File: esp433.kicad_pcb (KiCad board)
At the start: 2 copper layers, 47.1 x 72.6 mm, 50 parts, among them J1 USB_OTG, J2 CONN_01X03, Q1 MBT2222ADW1T1, SW1 SW_Push, U1 IRM-02-5, U2 AP2127K-3.3, U3 MAX7044, U4 ESP-12E, U5 FT231XS, Y1 Crystal

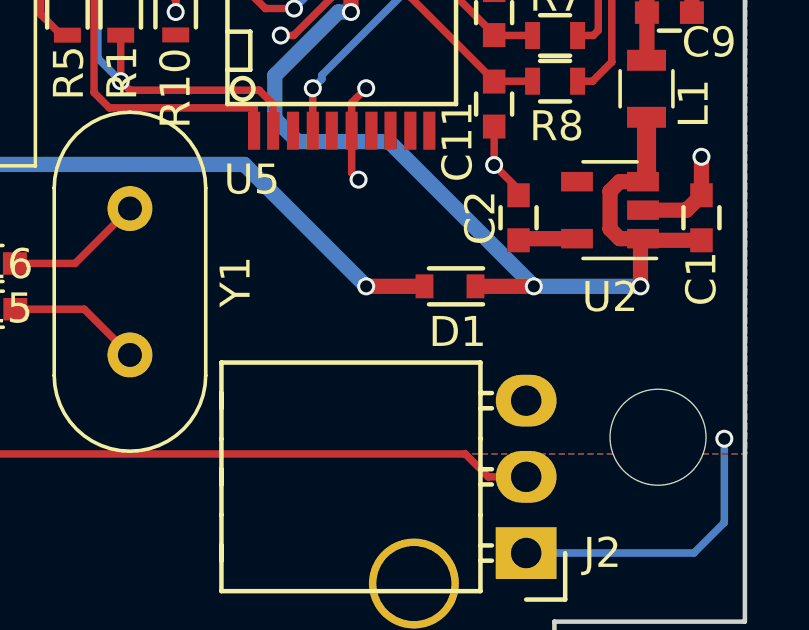
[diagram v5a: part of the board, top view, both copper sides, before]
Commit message: Fix footprint for D1
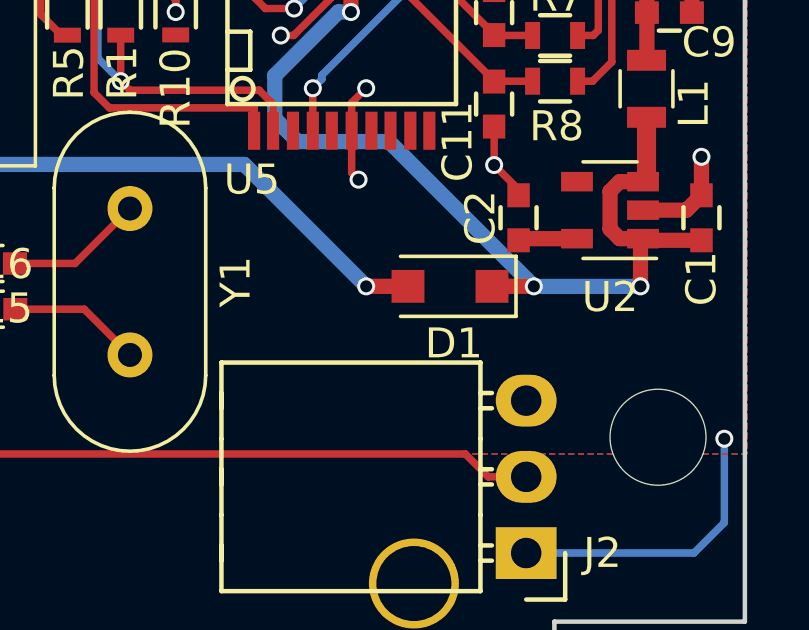
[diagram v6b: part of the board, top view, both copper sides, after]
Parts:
- D1: footprint Diodes_SMD:D_0603 -> Diodes_SMD:D_SOD-123F
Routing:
- net Net-(D1-Pad2): track 27.6 -> 27.1 mm
- net +5V: track 39.9 -> 39.3 mm
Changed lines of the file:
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@@
   (general
     (links 93)
-    (no_connects 6)
+    (no_connects 0)
     (area 90.679199 65.202999 137.920801 137.997001)
     (thickness 1.6)
@@
     )
   )
-  (module Diodes_SMD:D_0603 (layer F.Cu)
-    (at 128.016 120.396 180)
-    (descr "Diode SMD in 0603 package")
-    (tags "smd diode")
-    (attr smd)
-    (fp_text reference D1 (at -0.254 -1.524 180) (layer F.SilkS)
-      (effects (font (size 1 1) (thickness 0.15)))
-    )
-    (fp_text value D (at -2.032 0 180) (layer F.Fab)
-      (effects (font (size 1 1) (thickness 0.15)))
-    )
-    (fp_line (start 1.5 0.8) (end 1.5 -0.8) (layer F.CrtYd) (width 0.05))
-    (fp_line (start -1.5 0.8) (end 1.5 0.8) (layer F.CrtYd) (width 0.05))
-    (fp_line (start -1.5 -0.8) (end -1.5 0.8) (layer F.CrtYd) (width 0.05))
-    (fp_line (start 1.5 -0.8) (end -1.5 -0.8) (layer F.CrtYd) (width 0.05))
-    (fp_line (start 0.2 0) (end 0.4 0) (layer F.Fab) (width 0.15))
-    (fp_line (start -0.1 0) (end -0.3 0) (layer F.Fab) (width 0.15))
-    (fp_line (start -0.1 -0.2) (end -0.1 0.2) (layer F.Fab) (width 0.15))
-    (fp_line (start 0.2 0.2) (end 0.2 -0.2) (layer F.Fab) (width 0.15))
-    (fp_line (start -0.1 0) (end 0.2 0.2) (layer F.Fab) (width 0.15))
-    (fp_line (start 0.2 -0.2) (end -0.1 0) (layer F.Fab) (width 0.15))
-    (fp_line (start -0.8 0.5) (end -0.8 -0.5) (layer F.Fab) (width 0.15))
-    (fp_line (start 0.8 0.5) (end -0.8 0.5) (layer F.Fab) (width 0.15))
-    (fp_line (start 0.8 -0.5) (end 0.8 0.5) (layer F.Fab) (width 0.15))
-    (fp_line (start -0.8 -0.5) (end 0.8 -0.5) (layer F.Fab) (width 0.15))
-    (fp_line (start -1.1 0.6) (end 0.7 0.6) (layer F.SilkS) (width 0.15))
-    (fp_line (start -1.1 -0.6) (end 0.7 -0.6) (layer F.SilkS) (width 0.15))
-    (pad 1 smd rect (at -0.85 0 180) (size 0.6 0.8) (layers F.Cu F.Paste F.Mask)
-      (net 4 +5V))
-    (pad 2 smd rect (at 0.85 0 180) (size 0.6 0.8) (layers F.Cu F.Paste F.Mask)
-      (net 5 "Net-(D1-Pad2)"))
-  )
   (module LEDs:LED_0603 (layer F.Cu)
     (at 135.382 93.218 90)
@@
       (net 35 "Net-(C17-Pad1)"))
     (model Capacitors_SMD.3dshapes/C_0603.wrl
+      (at (xyz 0 0 0))
+      (scale (xyz 1 1 1))
+      (rotate (xyz 0 0 0))
+    )
+  )
+  (module Diodes_SMD:D_SOD-123F (layer F.Cu)
+    (at 128.016 120.396 180)
+    (descr D_SOD-123F)
+    (tags D_SOD-123F)
+    (attr smd)
+    (fp_text reference D1 (at -0.127 -1.905 180) (layer F.SilkS)
+      (effects (font (size 1 1) (thickness 0.15)))
+    )
+    (fp_text value D (at 0 2.1 180) (layer F.Fab)
+      (effects (font (size 1 1) (thickness 0.15)))
+    )
+    (fp_text user %R (at -0.127 -1.905 180) (layer F.Fab)
+      (effects (font (size 1 1) (thickness 0.15)))
+    )
+    (fp_line (start -2.2 -1) (end -2.2 1) (layer F.SilkS) (width 0.12))
+    (fp_line (start 0.25 0) (end 0.75 0) (layer F.Fab) (width 0.1))
+    (fp_line (start 0.25 0.4) (end -0.35 0) (layer F.Fab) (width 0.1))
+    (fp_line (start 0.25 -0.4) (end 0.25 0.4) (layer F.Fab) (width 0.1))
+    (fp_line (start -0.35 0) (end 0.25 -0.4) (layer F.Fab) (width 0.1))
+    (fp_line (start -0.35 0) (end -0.35 0.55) (layer F.Fab) (width 0.1))
+    (fp_line (start -0.35 0) (end -0.35 -0.55) (layer F.Fab) (width 0.1))
+    (fp_line (start -0.75 0) (end -0.35 0) (layer F.Fab) (width 0.1))
+    (fp_line (start -1.4 0.9) (end -1.4 -0.9) (layer F.Fab) (width 0.1))
+    (fp_line (start 1.4 0.9) (end -1.4 0.9) (layer F.Fab) (width 0.1))
+    (fp_line (start 1.4 -0.9) (end 1.4 0.9) (layer F.Fab) (width 0.1))
+    (fp_line (start -1.4 -0.9) (end 1.4 -0.9) (layer F.Fab) (width 0.1))
+    (fp_line (start -2.2 -1.15) (end 2.2 -1.15) (layer F.CrtYd) (width 0.05))
+    (fp_line (start 2.2 -1.15) (end 2.2 1.15) (layer F.CrtYd) (width 0.05))
+    (fp_line (start 2.2 1.15) (end -2.2 1.15) (layer F.CrtYd) (width 0.05))
+    (fp_line (start -2.2 -1.15) (end -2.2 1.15) (layer F.CrtYd) (width 0.05))
+    (fp_line (start -2.2 1) (end 1.65 1) (layer F.SilkS) (width 0.12))
+    (fp_line (start -2.2 -1) (end 1.65 -1) (layer F.SilkS) (width 0.12))
+    (pad 1 smd rect (at -1.4 0 180) (size 1.1 1.1) (layers F.Cu F.Paste F.Mask)
+      (net 4 +5V))
+    (pad 2 smd rect (at 1.4 0 180) (size 1.1 1.1) (layers F.Cu F.Paste F.Mask)
+      (net 5 "Net-(D1-Pad2)"))
+    (model ${KISYS3DMOD}/Diodes_SMD.3dshapes/D_SOD-123F.wrl
       (at (xyz 0 0 0))
       (scale (xyz 1 1 1))
@@
   (segment (start 130.769145 113.557891) (end 129.499145 113.557891) (width 0.25) (layer F.Cu) (net 3))
   (segment (start 129.499145 113.557891) (end 129.487145 113.569891) (width 0.25) (layer F.Cu) (net 3))
-  (segment (start 128.866 120.396) (end 130.81 120.396) (width 0.508) (layer F.Cu) (net 4))
+  (segment (start 130.81 120.396) (end 129.416 120.396) (width 0.508) (layer F.Cu) (net 4))
   (via (at 130.81 120.396) (size 0.6) (drill 0.4) (layers F.Cu B.Cu) (net 4))
   (segment (start 122.174 114.808) (end 122.936 115.57) (width 0.508) (layer B.Cu) (net 4))
@@
   (segment (start 124.525344 108.77789) (end 124.737345 108.989891) (width 0.381) (layer F.Cu) (net 4))
   (segment (start 123.945144 108.77789) (end 124.525344 108.77789) (width 0.381) (layer F.Cu) (net 4))
+  (segment (start 125.222 120.396) (end 126.616 120.396) (width 0.508) (layer F.Cu) (net 5))
   (segment (start 114.554 116.332) (end 121.158 116.332) (width 0.508) (layer B.Cu) (net 5))
   (via (at 125.222 120.396) (size 0.6) (drill 0.4) (layers F.Cu B.Cu) (net 5))
   (segment (start 114.554 116.332) (end 105.898 116.332) (width 0.508) (layer B.Cu) (net 5))
   (segment (start 105.898 116.332) (end 102.596 113.03) (width 0.508) (layer B.Cu) (net 5))
-  (segment (start 125.222 120.396) (end 127.166 120.396) (width 0.508) (layer F.Cu) (net 5))
   (segment (start 121.158 116.332) (end 125.222 120.396) (width 0.508) (layer B.Cu) (net 5))
   (segment (start 102.907 124.46) (end 104.431 122.936) (width 0.25) (layer F.Cu) (net 6))

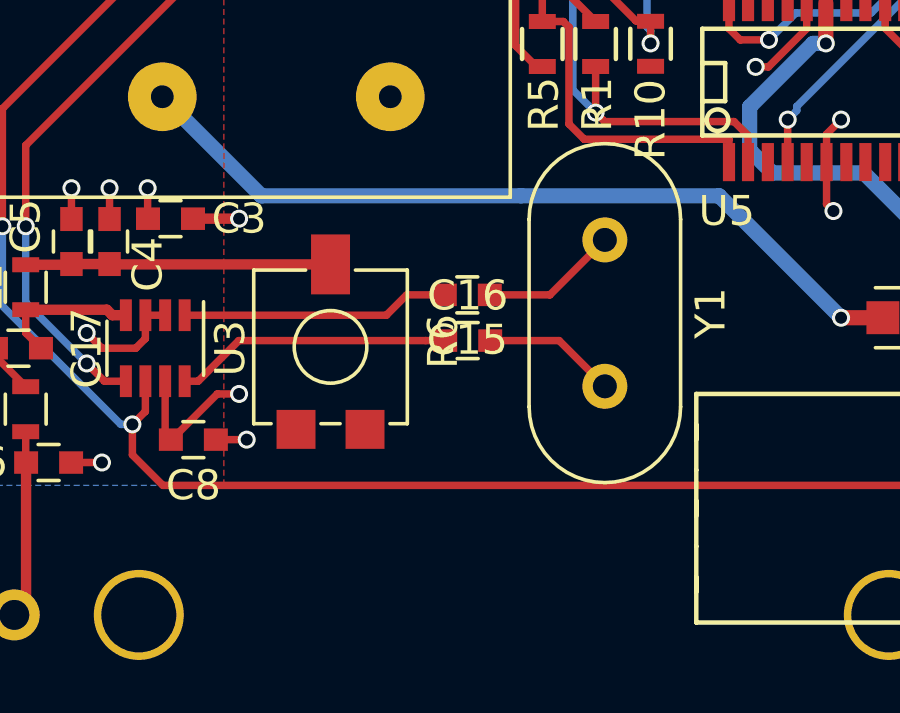
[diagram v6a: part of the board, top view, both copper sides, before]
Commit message: Add some dnp footprints for additional oscillator parallel capacitance
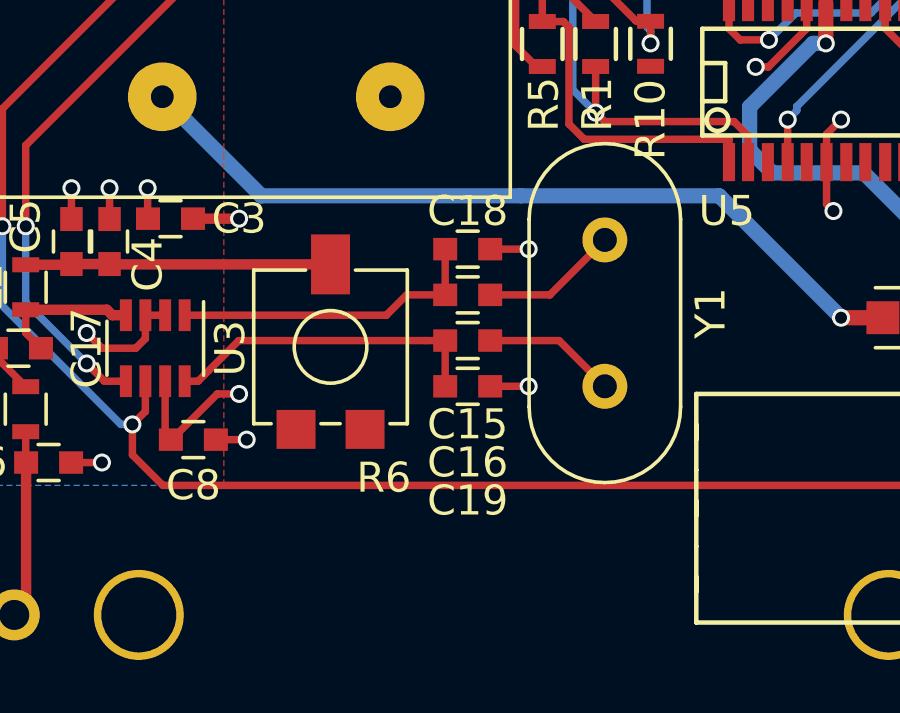
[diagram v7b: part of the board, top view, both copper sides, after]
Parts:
- added C18: DNP, Capacitors_SMD:C_0603, F.Cu at (112.8, 118.1)
- added C19: DNP, Capacitors_SMD:C_0603, F.Cu at (112.8, 122.7)
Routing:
- net GND: track 46.1 -> 48.7 mm, vias 21 -> 23
- net Net-(C15-Pad2): track 8.95 -> 10.5 mm
- net Net-(C16-Pad1): track 9.57 -> 11.1 mm
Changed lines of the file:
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@@
 (kicad_pcb (version 4) (host pcbnew 4.0.7)
   (general
-    (links 93)
-    (no_connects 0)
+    (links 97)
+    (no_connects 3)
     (area 90.679199 65.202999 137.920801 137.997001)
     (thickness 1.6)
-    (drawings 20)
-    (tracks 325)
+    (drawings 22)
+    (tracks 331)
     (zones 0)
-    (modules 50)
+    (modules 52)
     (nets 36)
   )
@@
     (tags "Spindle Trimmer Potentiometer   Vishay TS53YL")
     (attr smd)
-    (fp_text reference R6 (at -0.18 -3.75 270) (layer F.SilkS)
+    (fp_text reference R6 (at 4.362 -1.778 540) (layer F.SilkS)
       (effects (font (size 1 1) (thickness 0.15)))
     )
@@
   )
   (module Capacitors_SMD:C_0603 (layer F.Cu)
-    (at 112.764 119.634 180)
+    (at 112.776 119.634 180)
     (descr "Capacitor SMD 0603, reflow soldering, AVX (see smccp.pdf)")
     (tags "capacitor 0603")
     (attr smd)
-    (fp_text reference C15 (at 0 -1.5 180) (layer F.SilkS)
+    (fp_text reference C15 (at 0 -4.318 180) (layer F.SilkS)
       (effects (font (size 1 1) (thickness 0.15)))
     )
@@
     (tags "capacitor 0603")
     (attr smd)
-    (fp_text reference C16 (at 0 -1.5) (layer F.SilkS)
+    (fp_text reference C16 (at 0 4.064) (layer F.SilkS)
       (effects (font (size 1 1) (thickness 0.15)))
     )
@@
     )
   )
+  (module Capacitors_SMD:C_0603 (layer F.Cu)
+    (at 112.776 118.11 180)
+    (descr "Capacitor SMD 0603, reflow soldering, AVX (see smccp.pdf)")
+    (tags "capacitor 0603")
+    (attr smd)
+    (fp_text reference C18 (at 0 1.27 180) (layer F.SilkS)
+      (effects (font (size 1 1) (thickness 0.15)))
+    )
+    (fp_text value DNP (at 0 1.5 180) (layer F.Fab)
+      (effects (font (size 1 1) (thickness 0.15)))
+    )
+    (fp_line (start 1.4 0.65) (end -1.4 0.65) (layer F.CrtYd) (width 0.05))
+    (fp_line (start 1.4 0.65) (end 1.4 -0.65) (layer F.CrtYd) (width 0.05))
+    (fp_line (start -1.4 -0.65) (end -1.4 0.65) (layer F.CrtYd) (width 0.05))
+    (fp_line (start -1.4 -0.65) (end 1.4 -0.65) (layer F.CrtYd) (width 0.05))
+    (fp_line (start 0.35 0.6) (end -0.35 0.6) (layer F.SilkS) (width 0.12))
+    (fp_line (start -0.35 -0.6) (end 0.35 -0.6) (layer F.SilkS) (width 0.12))
+    (fp_line (start -0.8 -0.4) (end 0.8 -0.4) (layer F.Fab) (width 0.1))
+    (fp_line (start 0.8 -0.4) (end 0.8 0.4) (layer F.Fab) (width 0.1))
+    (fp_line (start 0.8 0.4) (end -0.8 0.4) (layer F.Fab) (width 0.1))
+    (fp_line (start -0.8 0.4) (end -0.8 -0.4) (layer F.Fab) (width 0.1))
+    (fp_text user %R (at 0 0 180) (layer F.Fab)
+      (effects (font (size 0.3 0.3) (thickness 0.075)))
+    )
+    (pad 2 smd rect (at 0.75 0 180) (size 0.8 0.75) (layers F.Cu F.Paste F.Mask)
+      (net 31 "Net-(C15-Pad2)"))
+    (pad 1 smd rect (at -0.75 0 180) (size 0.8 0.75) (layers F.Cu F.Paste F.Mask)
+      (net 1 GND))
+    (model Capacitors_SMD.3dshapes/C_0603.wrl
+      (at (xyz 0 0 0))
+      (scale (xyz 1 1 1))
+      (rotate (xyz 0 0 0))
+    )
+  )
+  (module Capacitors_SMD:C_0603 (layer F.Cu)
+    (at 112.776 122.682 180)
+    (descr "Capacitor SMD 0603, reflow soldering, AVX (see smccp.pdf)")
+    (tags "capacitor 0603")
+    (attr smd)
+    (fp_text reference C19 (at 0 -3.81 180) (layer F.SilkS)
+      (effects (font (size 1 1) (thickness 0.15)))
+    )
+    (fp_text value DNP (at 0 1.5 180) (layer F.Fab)
+      (effects (font (size 1 1) (thickness 0.15)))
+    )
+    (fp_line (start 1.4 0.65) (end -1.4 0.65) (layer F.CrtYd) (width 0.05))
+    (fp_line (start 1.4 0.65) (end 1.4 -0.65) (layer F.CrtYd) (width 0.05))
+    (fp_line (start -1.4 -0.65) (end -1.4 0.65) (layer F.CrtYd) (width 0.05))
+    (fp_line (start -1.4 -0.65) (end 1.4 -0.65) (layer F.CrtYd) (width 0.05))
+    (fp_line (start 0.35 0.6) (end -0.35 0.6) (layer F.SilkS) (width 0.12))
+    (fp_line (start -0.35 -0.6) (end 0.35 -0.6) (layer F.SilkS) (width 0.12))
+    (fp_line (start -0.8 -0.4) (end 0.8 -0.4) (layer F.Fab) (width 0.1))
+    (fp_line (start 0.8 -0.4) (end 0.8 0.4) (layer F.Fab) (width 0.1))
+    (fp_line (start 0.8 0.4) (end -0.8 0.4) (layer F.Fab) (width 0.1))
+    (fp_line (start -0.8 0.4) (end -0.8 -0.4) (layer F.Fab) (width 0.1))
+    (fp_text user %R (at 0 0 180) (layer F.Fab)
+      (effects (font (size 0.3 0.3) (thickness 0.075)))
+    )
+    (pad 2 smd rect (at 0.75 0 180) (size 0.8 0.75) (layers F.Cu F.Paste F.Mask)
+      (net 34 "Net-(C16-Pad1)"))
+    (pad 1 smd rect (at -0.75 0 180) (size 0.8 0.75) (layers F.Cu F.Paste F.Mask)
+      (net 1 GND))
+    (model Capacitors_SMD.3dshapes/C_0603.wrl
+      (at (xyz 0 0 0))
+      (scale (xyz 1 1 1))
+      (rotate (xyz 0 0 0))
+    )
+  )
+  (dimension 24.892 (width 0.3) (layer Dwgs.User)
+    (gr_text "24.892 mm" (at 80.554704 125.125681 90) (layer Dwgs.User)
+      (effects (font (size 1.5 1.5) (thickness 0.3)))
+    )
+    (feature1 (pts (xy 83.936704 112.679681) (xy 79.204704 112.679681)))
+    (feature2 (pts (xy 83.936704 137.571681) (xy 79.204704 137.571681)))
+    (crossbar (pts (xy 81.904704 137.571681) (xy 81.904704 112.679681)))
+    (arrow1a (pts (xy 81.904704 112.679681) (xy 82.491125 113.806185)))
+    (arrow1b (pts (xy 81.904704 112.679681) (xy 81.318283 113.806185)))
+    (arrow2a (pts (xy 81.904704 137.571681) (xy 82.491125 136.445177)))
+    (arrow2b (pts (xy 81.904704 137.571681) (xy 81.318283 136.445177)))
+  )
+  (dimension 32.004 (width 0.3) (layer Dwgs.User)
+    (gr_text "32.004 mm" (at 107.335992 141.554296) (layer Dwgs.User)
+      (effects (font (size 1.5 1.5) (thickness 0.3)))
+    )
+    (feature1 (pts (xy 123.337992 139.442297) (xy 123.337992 142.904296)))
+    (feature2 (pts (xy 91.333992 139.442297) (xy 91.333992 142.904296)))
+    (crossbar (pts (xy 91.333992 140.204296) (xy 123.337992 140.204296)))
+    (arrow1a (pts (xy 123.337992 140.204296) (xy 122.211488 140.790717)))
+    (arrow1b (pts (xy 123.337992 140.204296) (xy 122.211488 139.617875)))
+    (arrow2a (pts (xy 91.333992 140.204296) (xy 92.460496 140.790717)))
+    (arrow2b (pts (xy 91.333992 140.204296) (xy 92.460496 139.617875)))
+  )
   (gr_line (start 131.4958 131.572) (end 137.8458 131.572) (layer Edge.Cuts) (width 0.15))
   (gr_line (start 131.4958 137.922) (end 131.4958 131.572) (layer Edge.Cuts) (width 0.15))
@@
   (gr_line (start 97.1042 137.922) (end 131.4958 137.922) (layer Edge.Cuts) (width 0.15))
   (gr_line (start 97.1042 65.278) (end 131.4958 65.278) (layer Edge.Cuts) (width 0.15))
+  (segment (start 113.526 122.682) (end 114.808 122.682) (width 0.25) (layer F.Cu) (net 1))
+  (via (at 114.808 122.682) (size 0.6) (drill 0.4) (layers F.Cu B.Cu) (net 1))
+  (segment (start 113.526 118.11) (end 114.808 118.11) (width 0.25) (layer F.Cu) (net 1))
+  (via (at 114.808 118.11) (size 0.6) (drill 0.4) (layers F.Cu B.Cu) (net 1))
   (segment (start 95.504 119.9) (end 95.504 118.872) (width 0.25) (layer F.Cu) (net 1))
   (via (at 95.504 118.872) (size 0.6) (drill 0.4) (layers F.Cu B.Cu) (net 1))
@@
   (segment (start 97.052 121.702) (end 98.044 122.694) (width 0.25) (layer F.Cu) (net 30))
   (segment (start 98.032 122.682) (end 98.044 122.694) (width 0.25) (layer F.Cu) (net 30))
+  (segment (start 112.026 119.634) (end 112.026 118.11) (width 0.25) (layer F.Cu) (net 31))
+  (segment (start 110.744 119.634) (end 112.026 119.634) (width 0.25) (layer F.Cu) (net 31))
   (segment (start 110.066 120.312) (end 110.744 119.634) (width 0.25) (layer F.Cu) (net 31))
-  (segment (start 110.744 119.634) (end 112.014 119.634) (width 0.25) (layer F.Cu) (net 31))
   (segment (start 103.342 120.312) (end 110.066 120.312) (width 0.25) (layer F.Cu) (net 31))
-  (segment (start 113.514 119.634) (end 115.516 119.634) (width 0.25) (layer F.Cu) (net 32))
+  (segment (start 113.526 119.634) (end 115.516 119.634) (width 0.25) (layer F.Cu) (net 32))
   (segment (start 115.516 119.634) (end 117.348 117.802) (width 0.25) (layer F.Cu) (net 32))
   (segment (start 113.526 121.158) (end 115.824 121.158) (width 0.25) (layer F.Cu) (net 33))
   (segment (start 115.824 121.158) (end 117.348 122.682) (width 0.25) (layer F.Cu) (net 33))
+  (segment (start 112.026 121.158) (end 112.026 122.682) (width 0.25) (layer F.Cu) (net 34))
   (segment (start 103.342 122.512) (end 103.792 122.512) (width 0.25) (layer F.Cu) (net 34))
   (segment (start 103.792 122.512) (end 105.146 121.158) (width 0.25) (layer F.Cu) (net 34))

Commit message: Updated netlist in pcb, no change to layout
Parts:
- C3: value 100n -> DNP
- C5: value 680p -> 0.01u
- L3: value 15nH -> 16nH
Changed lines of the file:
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@@
   (general
     (links 97)
-    (no_connects 3)
+    (no_connects 0)
     (area 90.679199 65.202999 137.920801 137.997001)
     (thickness 1.6)
-    (drawings 22)
+    (drawings 20)
     (tracks 331)
     (zones 0)
@@
       (effects (font (size 1 1) (thickness 0.15)))
     )
-    (fp_text value 100n (at 0 1.5 180) (layer F.Fab)
+    (fp_text value DNP (at 0 1.5 180) (layer F.Fab)
       (effects (font (size 1 1) (thickness 0.15)))
     )
@@
       (effects (font (size 1 1) (thickness 0.15)))
     )
-    (fp_text value 680p (at 0 1.5 90) (layer F.Fab)
+    (fp_text value 0.01u (at 0 1.5 90) (layer F.Fab)
       (effects (font (size 1 1) (thickness 0.15)))
     )
@@
       (effects (font (size 1 1) (thickness 0.15)))
     )
-    (fp_text value 15nH (at 0 1.9 270) (layer F.Fab)
+    (fp_text value 16nH (at 0 1.9 270) (layer F.Fab)
       (effects (font (size 1 1) (thickness 0.15)))
     )
@@
     )
   )
-  (dimension 24.892 (width 0.3) (layer Dwgs.User)
-    (gr_text "24.892 mm" (at 80.554704 125.125681 90) (layer Dwgs.User)
-      (effects (font (size 1.5 1.5) (thickness 0.3)))
-    )
-    (feature1 (pts (xy 83.936704 112.679681) (xy 79.204704 112.679681)))
-    (feature2 (pts (xy 83.936704 137.571681) (xy 79.204704 137.571681)))
-    (crossbar (pts (xy 81.904704 137.571681) (xy 81.904704 112.679681)))
-    (arrow1a (pts (xy 81.904704 112.679681) (xy 82.491125 113.806185)))
-    (arrow1b (pts (xy 81.904704 112.679681) (xy 81.318283 113.806185)))
-    (arrow2a (pts (xy 81.904704 137.571681) (xy 82.491125 136.445177)))
-    (arrow2b (pts (xy 81.904704 137.571681) (xy 81.318283 136.445177)))
-  )
-  (dimension 32.004 (width 0.3) (layer Dwgs.User)
-    (gr_text "32.004 mm" (at 107.335992 141.554296) (layer Dwgs.User)
-      (effects (font (size 1.5 1.5) (thickness 0.3)))
-    )
-    (feature1 (pts (xy 123.337992 139.442297) (xy 123.337992 142.904296)))
-    (feature2 (pts (xy 91.333992 139.442297) (xy 91.333992 142.904296)))
-    (crossbar (pts (xy 91.333992 140.204296) (xy 123.337992 140.204296)))
-    (arrow1a (pts (xy 123.337992 140.204296) (xy 122.211488 140.790717)))
-    (arrow1b (pts (xy 123.337992 140.204296) (xy 122.211488 139.617875)))
-    (arrow2a (pts (xy 91.333992 140.204296) (xy 92.460496 140.790717)))
-    (arrow2b (pts (xy 91.333992 140.204296) (xy 92.460496 139.617875)))
-  )
   (gr_line (start 131.4958 131.572) (end 137.8458 131.572) (layer Edge.Cuts) (width 0.15))
